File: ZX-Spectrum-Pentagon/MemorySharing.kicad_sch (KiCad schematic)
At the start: 16 parts

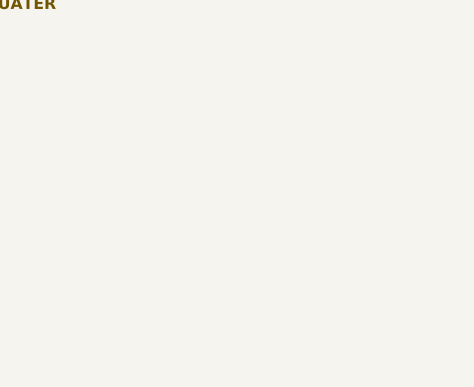
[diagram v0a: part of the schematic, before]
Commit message: reuse units of ic
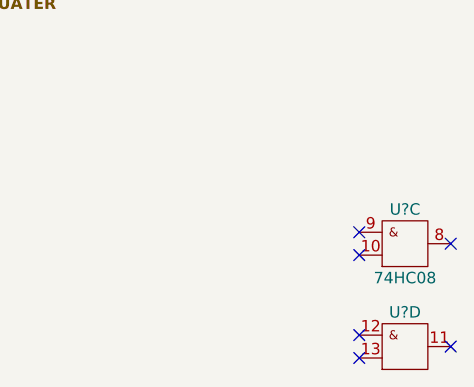
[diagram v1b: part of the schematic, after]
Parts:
- added U?: 74HC08, Package_DIP:DIP-14_W7.62mm, symbol 74IEC:74HC08
- added U?: ~, symbol 74IEC:74HC08
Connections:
- net GND: now also U?.7 (GND), U?.7 (GND)
- net VCC: now also U?.14 (VCC), U?.14 (VCC)
- no-connect marks 0 -> 6
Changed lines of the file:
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@@
   (junction (at 129.54 86.36) (diameter 0) (color 0 0 0 0)
   )
+  (no_connect (at 196.85 138.43))
+  (no_connect (at 196.85 140.97))
+  (no_connect (at 207.01 139.7))
+  (no_connect (at 207.01 151.13))
+  (no_connect (at 196.85 149.86))
+  (no_connect (at 196.85 152.4))
   (wire (pts (xy 58.42 86.36) (xy 101.6 86.36))
     (stroke (width 0) (type default) (color 0 0 0 0))
@@
     (pin "9")
   )
+  (symbol (lib_id "74IEC:74HC08") (at 201.93 139.7 0) (unit 3)
+    (in_bom yes) (on_board no)
+    (property "Reference" "U?" (id 0) (at 201.93 135.89 0))
+    (property "Value" "74HC08" (id 1) (at 201.93 143.51 0))
+    (property "Footprint" "Package_DIP:DIP-14_W7.62mm" (id 2) (at 201.93 147.32 0)
+      (effects (font (size 1.27 1.27)) hide)
+    )
+    (property "Datasheet" "https://www.ti.com/lit/ug/scyd013b/scyd013b.pdf" (id 3) (at 201.93 135.89 0)
+      (effects (font (size 1.27 1.27)) hide)
+    )
+    (pin "14")
+    (pin "7")
+    (pin "1")
+    (pin "2")
+    (pin "3")
+    (pin "4")
+    (pin "5")
+    (pin "6")
+    (pin "10")
+    (pin "8")
+    (pin "9")
+    (pin "11")
+    (pin "12")
+    (pin "13")
+  )
+  (symbol (lib_id "74IEC:74HC08") (at 201.93 151.13 0) (unit 4)
+    (in_bom yes) (on_board no)
+    (property "Reference" "U?" (id 0) (at 201.93 147.32 0))
+    (property "Value" "~" (id 1) (at 201.93 154.94 0))
+    (property "Footprint" "" (id 2) (at 201.93 158.75 0)
+      (effects (font (size 1.27 1.27)) hide)
+    )
+    (property "Datasheet" "https://www.ti.com/lit/ug/scyd013b/scyd013b.pdf" (id 3) (at 201.93 147.32 0)
+      (effects (font (size 1.27 1.27)) hide)
+    )
+    (pin "14")
+    (pin "7")
+    (pin "1")
+    (pin "2")
+    (pin "3")
+    (pin "4")
+    (pin "5")
+    (pin "6")
+    (pin "10")
+    (pin "8")
+    (pin "9")
+    (pin "11")
+    (pin "12")
+    (pin "13")
+  )
 )

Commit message: annotate
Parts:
- gave numbers to parts that had none: 10
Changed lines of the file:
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@@
   (symbol (lib_id "74IEC:74HC04") (at 121.92 41.91 0) (unit 5)
     (in_bom yes) (on_board yes)
-    (property "Reference" "U?" (id 0) (at 121.92 38.1 0))
+    (property "Reference" "U7" (id 0) (at 121.92 38.1 0))
     (property "Value" "74HC04" (id 1) (at 121.92 45.72 0))
     (property "Footprint" "Package_DIP:DIP-14_W7.62mm" (id 2) (at 121.92 36.576 0)
@@
   (symbol (lib_id "74IEC:74HC04") (at 53.34 102.87 0) (unit 6)
     (in_bom yes) (on_board yes)
-    (property "Reference" "U?" (id 0) (at 53.34 99.06 0))
+    (property "Reference" "U7" (id 0) (at 53.34 99.06 0))
     (property "Value" "74HC04" (id 1) (at 53.34 106.68 0))
     (property "Footprint" "Package_DIP:DIP-14_W7.62mm" (id 2) (at 53.34 97.536 0)
@@
   (symbol (lib_id "74IEC:74HC00") (at 71.12 40.64 0) (unit 1)
     (in_bom yes) (on_board yes)
-    (property "Reference" "U?" (id 0) (at 71.12 36.83 0))
+    (property "Reference" "U32" (id 0) (at 71.12 36.83 0))
     (property "Value" "74HC00" (id 1) (at 71.12 44.45 0))
     (property "Footprint" "Package_DIP:DIP-14_W7.62mm" (id 2) (at 71.12 46.99 0)
@@
   (symbol (lib_id "74IEC:74HC00") (at 86.36 26.67 0) (unit 4)
     (in_bom yes) (on_board yes)
-    (property "Reference" "U?" (id 0) (at 86.36 22.86 0))
+    (property "Reference" "U8" (id 0) (at 86.36 22.86 0))
     (property "Value" "74HC00" (id 1) (at 86.36 30.48 0))
     (property "Footprint" "Package_DIP:DIP-14_W7.62mm" (id 2) (at 86.36 33.02 0)
@@
   (symbol (lib_id "74IEC:74HC00") (at 137.16 92.71 0) (unit 4)
     (in_bom yes) (on_board yes)
-    (property "Reference" "U?" (id 0) (at 137.16 88.9 0))
+    (property "Reference" "U32" (id 0) (at 137.16 88.9 0))
     (property "Value" "74HC00" (id 1) (at 137.16 96.52 0))
     (property "Footprint" "Package_DIP:DIP-14_W7.62mm" (id 2) (at 137.16 99.06 0)
@@
   (symbol (lib_id "74IEC:74HC00") (at 92.71 50.8 0) (unit 2)
     (in_bom yes) (on_board yes)
-    (property "Reference" "U?" (id 0) (at 92.71 46.99 0))
+    (property "Reference" "U32" (id 0) (at 92.71 46.99 0))
     (property "Value" "74HC00" (id 1) (at 92.71 54.61 0))
     (property "Footprint" "Package_DIP:DIP-14_W7.62mm" (id 2) (at 92.71 57.15 0)
@@
   (symbol (lib_id "74IEC:74HC00") (at 137.16 78.74 0) (unit 3)
     (in_bom yes) (on_board yes)
-    (property "Reference" "U?" (id 0) (at 137.16 74.93 0))
+    (property "Reference" "U32" (id 0) (at 137.16 74.93 0))
     (property "Value" "74HC00" (id 1) (at 137.16 82.55 0))
     (property "Footprint" "Package_DIP:DIP-14_W7.62mm" (id 2) (at 137.16 85.09 0)
@@
   (symbol (lib_id "74IEC:74HC02") (at 109.22 41.91 0) (unit 4)
     (in_bom yes) (on_board yes)
-    (property "Reference" "U?" (id 0) (at 109.22 38.1 0))
+    (property "Reference" "U11" (id 0) (at 109.22 38.1 0))
     (property "Value" "74HC02" (id 1) (at 109.22 45.72 0))
     (property "Footprint" "Package_DIP:DIP-14_W7.62mm" (id 2) (at 109.22 49.53 0)
@@
   (symbol (lib_id "74IEC:74HC08") (at 68.58 104.14 0) (unit 2)
     (in_bom yes) (on_board yes)
-    (property "Reference" "U?" (id 0) (at 68.58 100.33 0))
+    (property "Reference" "U34" (id 0) (at 68.58 100.33 0))
     (property "Value" "74HC08" (id 1) (at 68.58 107.95 0))
     (property "Footprint" "Package_DIP:DIP-14_W7.62mm" (id 2) (at 68.58 111.76 0)
@@
   (symbol (lib_id "74IEC:74HC08") (at 97.79 93.98 0) (unit 1)
     (in_bom yes) (on_board yes)
-    (property "Reference" "U?" (id 0) (at 97.79 90.17 0))
+    (property "Reference" "U34" (id 0) (at 97.79 90.17 0))
     (property "Value" "74HC08" (id 1) (at 97.79 97.79 0))
     (property "Footprint" "Package_DIP:DIP-14_W7.62mm" (id 2) (at 97.79 101.6 0)
@@
   (symbol (lib_id "74IEC:74HC04") (at 71.12 25.4 0) (unit 4)
     (in_bom yes) (on_board yes)
-    (property "Reference" "U?" (id 0) (at 71.12 21.59 0))
+    (property "Reference" "U7" (id 0) (at 71.12 21.59 0))
     (property "Value" "74HC04" (id 1) (at 71.12 29.21 0))
     (property "Footprint" "Package_DIP:DIP-14_W7.62mm" (id 2) (at 71.12 20.066 0)
@@
   (symbol (lib_id "74IEC:74HC86") (at 93.98 78.74 0) (unit 3)
     (in_bom yes) (on_board yes)
-    (property "Reference" "U?" (id 0) (at 93.98 74.93 0))
+    (property "Reference" "U9" (id 0) (at 93.98 74.93 0))
     (property "Value" "74HC86" (id 1) (at 93.98 82.55 0))
     (property "Footprint" "Package_DIP:DIP-14_W7.62mm" (id 2) (at 93.98 86.36 0)
@@
   (symbol (lib_id "74IEC:74HC11") (at 50.8 76.2 0) (unit 3)
     (in_bom yes) (on_board yes)
-    (property "Reference" "U?" (id 0) (at 50.8 71.12 0))
+    (property "Reference" "U4" (id 0) (at 50.8 71.12 0))
     (property "Value" "74HC11" (id 1) (at 50.8 81.28 0))
     (property "Footprint" "Package_DIP:DIP-14_W7.62mm" (id 2) (at 50.8 71.12 0)
@@
   (symbol (lib_id "74IEC:74HC32") (at 53.34 113.03 0) (unit 3)
     (in_bom yes) (on_board yes)
-    (property "Reference" "U?" (id 0) (at 53.34 109.22 0))
+    (property "Reference" "U31" (id 0) (at 53.34 109.22 0))
     (property "Value" "74HC32" (id 1) (at 53.34 116.84 0))
     (property "Footprint" "Package_DIP:DIP-14_W7.62mm" (id 2) (at 53.34 120.65 0)
@@
   (symbol (lib_id "power:VCC") (at 60.96 71.12 0) (unit 1)
     (in_bom yes) (on_board yes)
-    (property "Reference" "#PWR?" (id 0) (at 60.96 74.93 0)
+    (property "Reference" "#PWR051" (id 0) (at 60.96 74.93 0)
       (effects (font (size 1.27 1.27)) hide)
     )
@@
   (symbol (lib_id "power:VCC") (at 104.14 73.66 0) (unit 1)
     (in_bom yes) (on_board yes)
-    (property "Reference" "#PWR?" (id 0) (at 104.14 77.47 0)
+    (property "Reference" "#PWR052" (id 0) (at 104.14 77.47 0)
       (effects (font (size 1.27 1.27)) hide)
     )
@@
   (symbol (lib_id "74IEC:74HC74") (at 71.12 77.47 0) (unit 1)
     (in_bom yes) (on_board yes)
-    (property "Reference" "U?" (id 0) (at 71.12 71.12 0))
+    (property "Reference" "U33" (id 0) (at 71.12 71.12 0))
     (property "Value" "74HC74" (id 1) (at 71.12 83.82 0))
     (property "Footprint" "Package_DIP:DIP-14_W7.62mm" (id 2) (at 71.12 71.12 0)
@@
   (symbol (lib_id "74IEC:74HC74") (at 114.3 80.01 0) (unit 2)
     (in_bom yes) (on_board yes)
-    (property "Reference" "U?" (id 0) (at 114.3 73.66 0))
+    (property "Reference" "U33" (id 0) (at 114.3 73.66 0))
     (property "Value" "74HC74" (id 1) (at 114.3 86.36 0))
     (property "Footprint" "Package_DIP:DIP-14_W7.62mm" (id 2) (at 114.3 73.66 0)
@@
   (symbol (lib_id "74IEC:74HC08") (at 201.93 139.7 0) (unit 3)
     (in_bom yes) (on_board no)
-    (property "Reference" "U?" (id 0) (at 201.93 135.89 0))
+    (property "Reference" "U34" (id 0) (at 201.93 135.89 0))
     (property "Value" "74HC08" (id 1) (at 201.93 143.51 0))
     (property "Footprint" "Package_DIP:DIP-14_W7.62mm" (id 2) (at 201.93 147.32 0)
@@
   (symbol (lib_id "74IEC:74HC08") (at 201.93 151.13 0) (unit 4)
     (in_bom yes) (on_board no)
-    (property "Reference" "U?" (id 0) (at 201.93 147.32 0))
+    (property "Reference" "U35" (id 0) (at 201.93 147.32 0))
     (property "Value" "~" (id 1) (at 201.93 154.94 0))
     (property "Footprint" "" (id 2) (at 201.93 158.75 0)

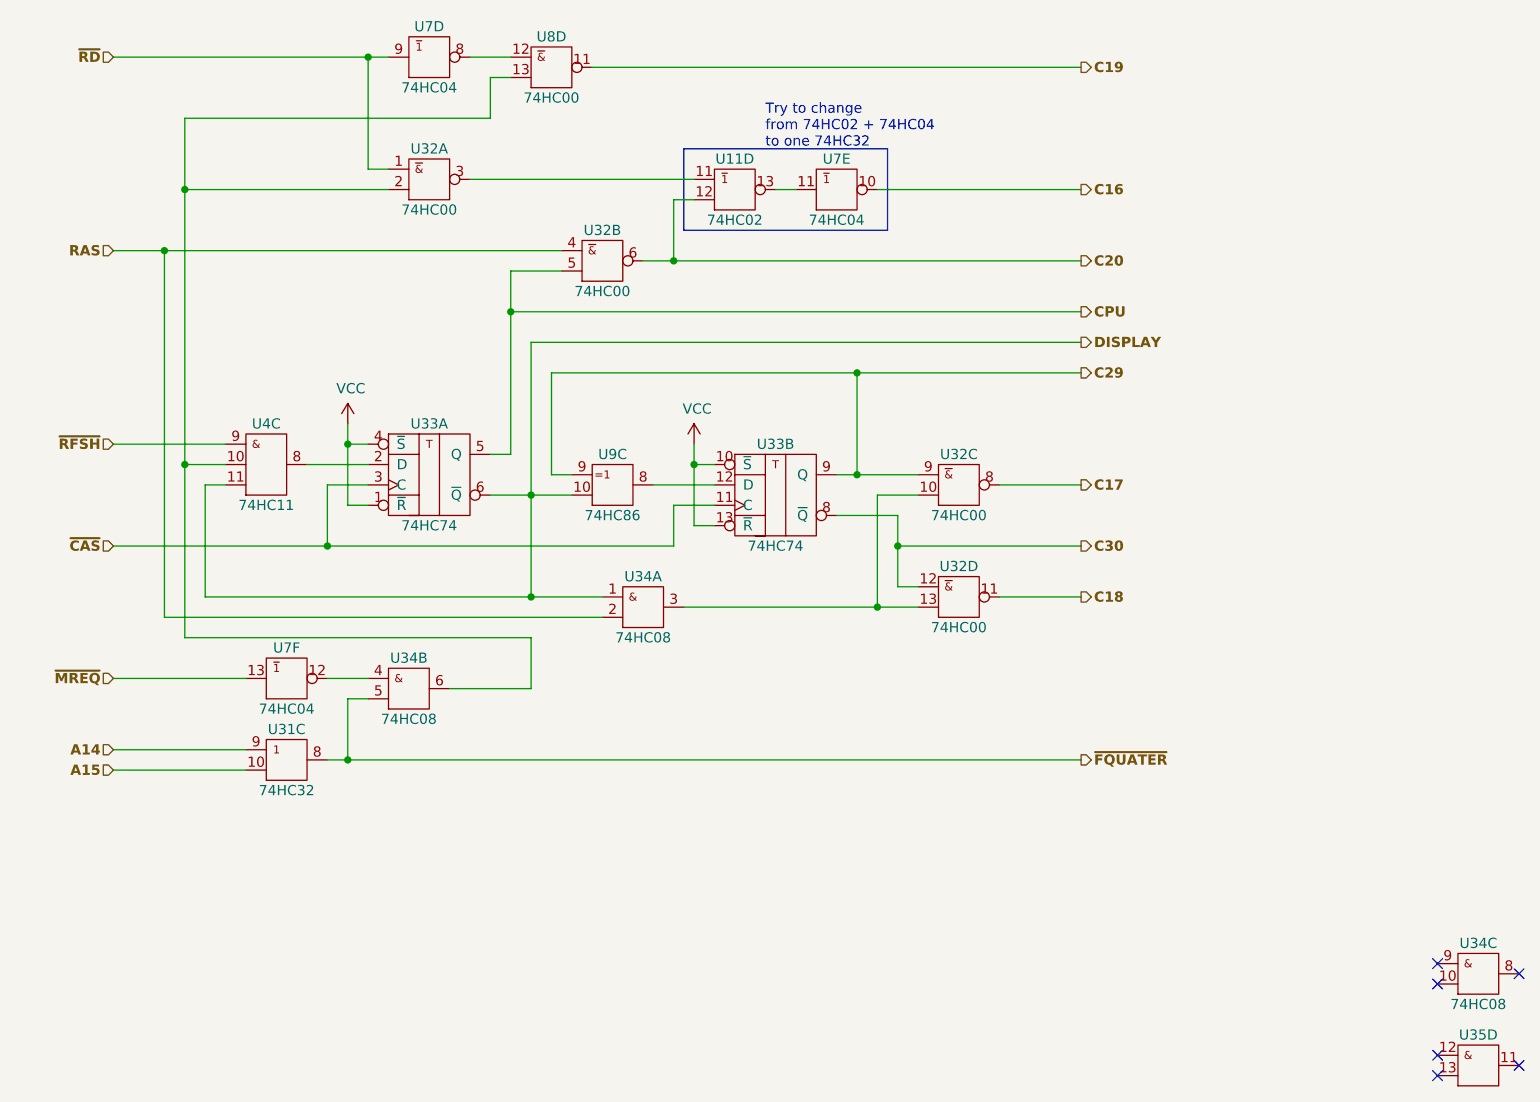
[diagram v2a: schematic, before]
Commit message: delete unuser labels fix problem with units
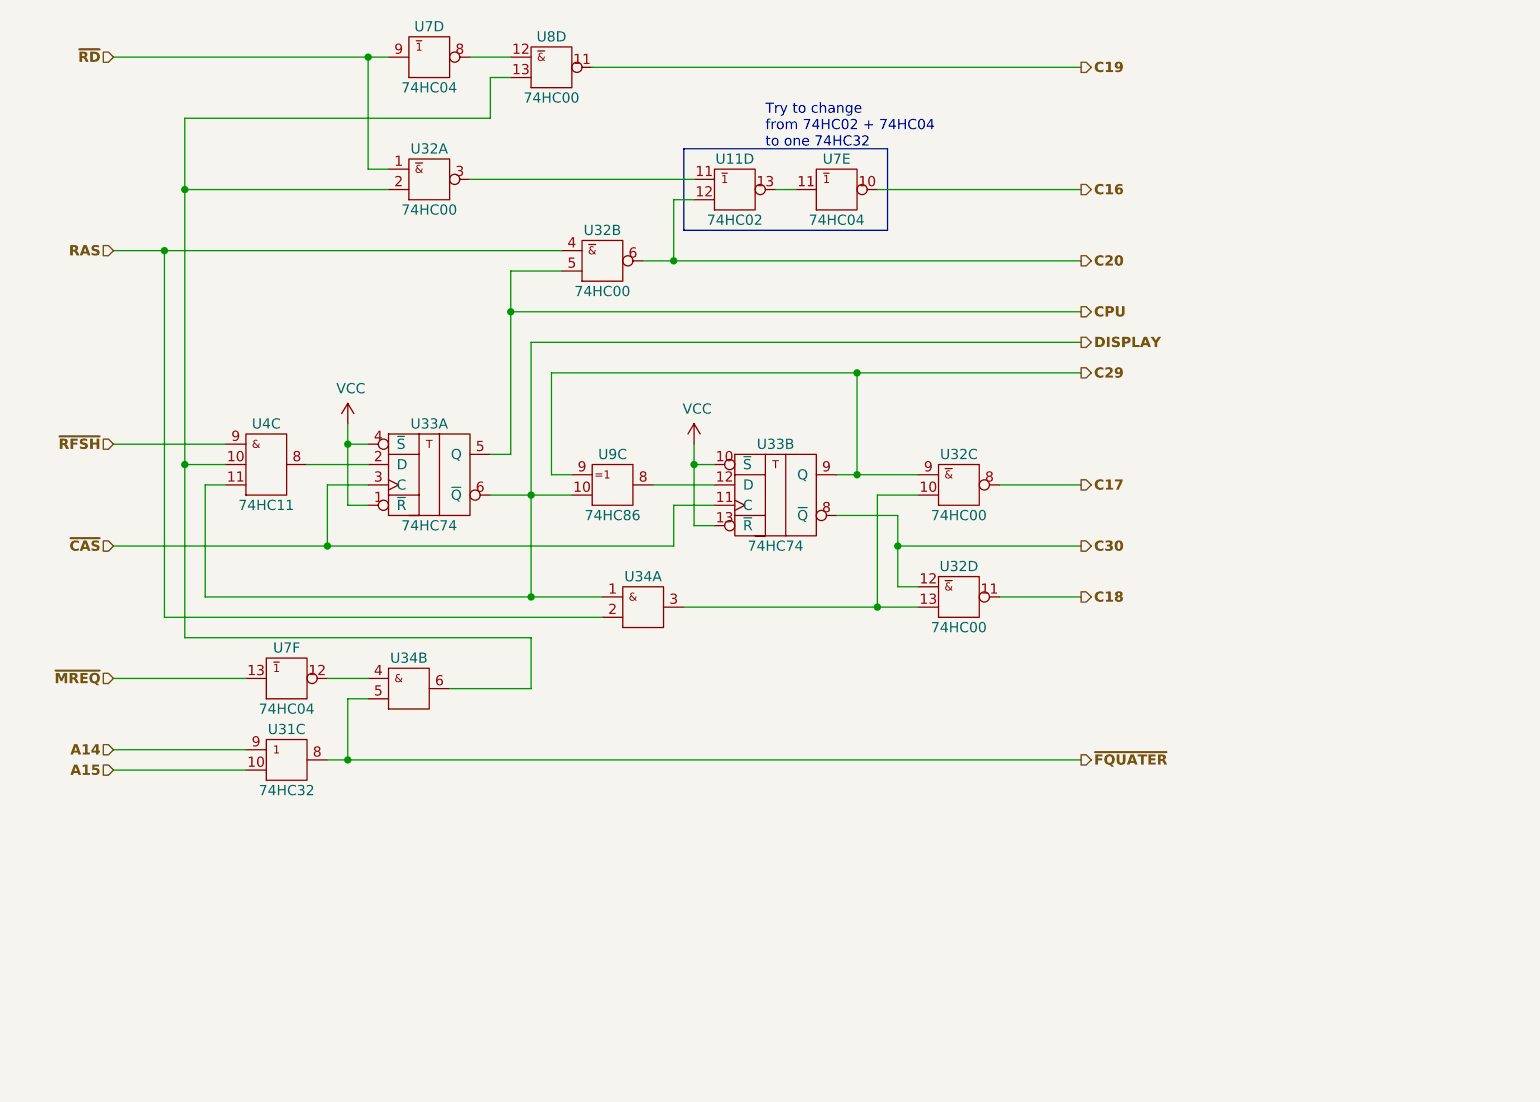
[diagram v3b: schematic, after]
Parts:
- removed unit 3 of U34
- removed U35: ~, symbol 74IEC:74HC08
- U34: value 74HC08 -> (none); footprint Package_DIP:DIP-14_W7.62mm -> (none)
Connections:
- no-connect marks 6 -> 0
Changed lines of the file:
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@@
   (junction (at 129.54 86.36) (diameter 0) (color 0 0 0 0)
   )
-  (no_connect (at 196.85 138.43))
-  (no_connect (at 196.85 140.97))
-  (no_connect (at 207.01 139.7))
-  (no_connect (at 207.01 151.13))
-  (no_connect (at 196.85 149.86))
-  (no_connect (at 196.85 152.4))
   (wire (pts (xy 58.42 86.36) (xy 101.6 86.36))
     (stroke (width 0) (type default) (color 0 0 0 0))
@@
     (in_bom yes) (on_board yes)
     (property "Reference" "U34" (id 0) (at 68.58 100.33 0))
-    (property "Value" "74HC08" (id 1) (at 68.58 107.95 0))
-    (property "Footprint" "Package_DIP:DIP-14_W7.62mm" (id 2) (at 68.58 111.76 0)
+    (property "Value" "" (id 1) (at 68.58 107.95 0))
+    (property "Footprint" "" (id 2) (at 68.58 111.76 0)
       (effects (font (size 1.27 1.27)) hide)
     )
@@
     (in_bom yes) (on_board yes)
     (property "Reference" "U34" (id 0) (at 97.79 90.17 0))
-    (property "Value" "74HC08" (id 1) (at 97.79 97.79 0))
-    (property "Footprint" "Package_DIP:DIP-14_W7.62mm" (id 2) (at 97.79 101.6 0)
+    (property "Value" "" (id 1) (at 97.79 97.79 0))
+    (property "Footprint" "" (id 2) (at 97.79 101.6 0)
       (effects (font (size 1.27 1.27)) hide)
     )
@@
     (pin "9")
   )
-  (symbol (lib_id "74IEC:74HC08") (at 201.93 139.7 0) (unit 3)
-    (in_bom yes) (on_board no)
-    (property "Reference" "U34" (id 0) (at 201.93 135.89 0))
-    (property "Value" "74HC08" (id 1) (at 201.93 143.51 0))
-    (property "Footprint" "Package_DIP:DIP-14_W7.62mm" (id 2) (at 201.93 147.32 0)
-      (effects (font (size 1.27 1.27)) hide)
-    )
-    (property "Datasheet" "https://www.ti.com/lit/ug/scyd013b/scyd013b.pdf" (id 3) (at 201.93 135.89 0)
-      (effects (font (size 1.27 1.27)) hide)
-    )
-    (pin "14")
-    (pin "7")
-    (pin "1")
-    (pin "2")
-    (pin "3")
-    (pin "4")
-    (pin "5")
-    (pin "6")
-    (pin "10")
-    (pin "8")
-    (pin "9")
-    (pin "11")
-    (pin "12")
-    (pin "13")
-  )
-  (symbol (lib_id "74IEC:74HC08") (at 201.93 151.13 0) (unit 4)
-    (in_bom yes) (on_board no)
-    (property "Reference" "U35" (id 0) (at 201.93 147.32 0))
-    (property "Value" "~" (id 1) (at 201.93 154.94 0))
-    (property "Footprint" "" (id 2) (at 201.93 158.75 0)
-      (effects (font (size 1.27 1.27)) hide)
-    )
-    (property "Datasheet" "https://www.ti.com/lit/ug/scyd013b/scyd013b.pdf" (id 3) (at 201.93 147.32 0)
-      (effects (font (size 1.27 1.27)) hide)
-    )
-    (pin "14")
-    (pin "7")
-    (pin "1")
-    (pin "2")
-    (pin "3")
-    (pin "4")
-    (pin "5")
-    (pin "6")
-    (pin "10")
-    (pin "8")
-    (pin "9")
-    (pin "11")
-    (pin "12")
-    (pin "13")
-  )
 )

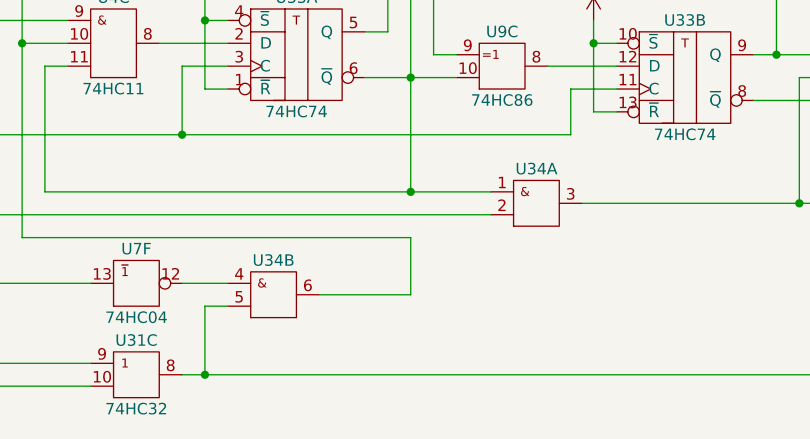
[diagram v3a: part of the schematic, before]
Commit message: chsnge some signals Make a track between CPU and buffers
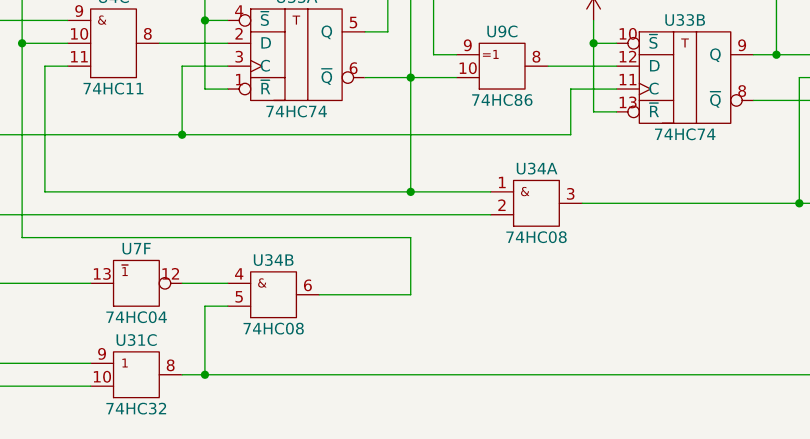
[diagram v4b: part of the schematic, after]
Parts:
- U34: value (none) -> 74HC08; footprint (none) -> Package_DIP:DIP-14_W7.62mm
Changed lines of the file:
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@@
     (in_bom yes) (on_board yes)
     (property "Reference" "U34" (id 0) (at 68.58 100.33 0))
-    (property "Value" "" (id 1) (at 68.58 107.95 0))
-    (property "Footprint" "" (id 2) (at 68.58 111.76 0)
+    (property "Value" "74HC08" (id 1) (at 68.58 107.95 0))
+    (property "Footprint" "Package_DIP:DIP-14_W7.62mm" (id 2) (at 68.58 111.76 0)
       (effects (font (size 1.27 1.27)) hide)
     )
@@
     (in_bom yes) (on_board yes)
     (property "Reference" "U34" (id 0) (at 97.79 90.17 0))
-    (property "Value" "" (id 1) (at 97.79 97.79 0))
-    (property "Footprint" "" (id 2) (at 97.79 101.6 0)
+    (property "Value" "74HC08" (id 1) (at 97.79 97.79 0))
+    (property "Footprint" "Package_DIP:DIP-14_W7.62mm" (id 2) (at 97.79 101.6 0)
       (effects (font (size 1.27 1.27)) hide)
     )
